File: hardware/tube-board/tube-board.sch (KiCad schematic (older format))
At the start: 8 parts

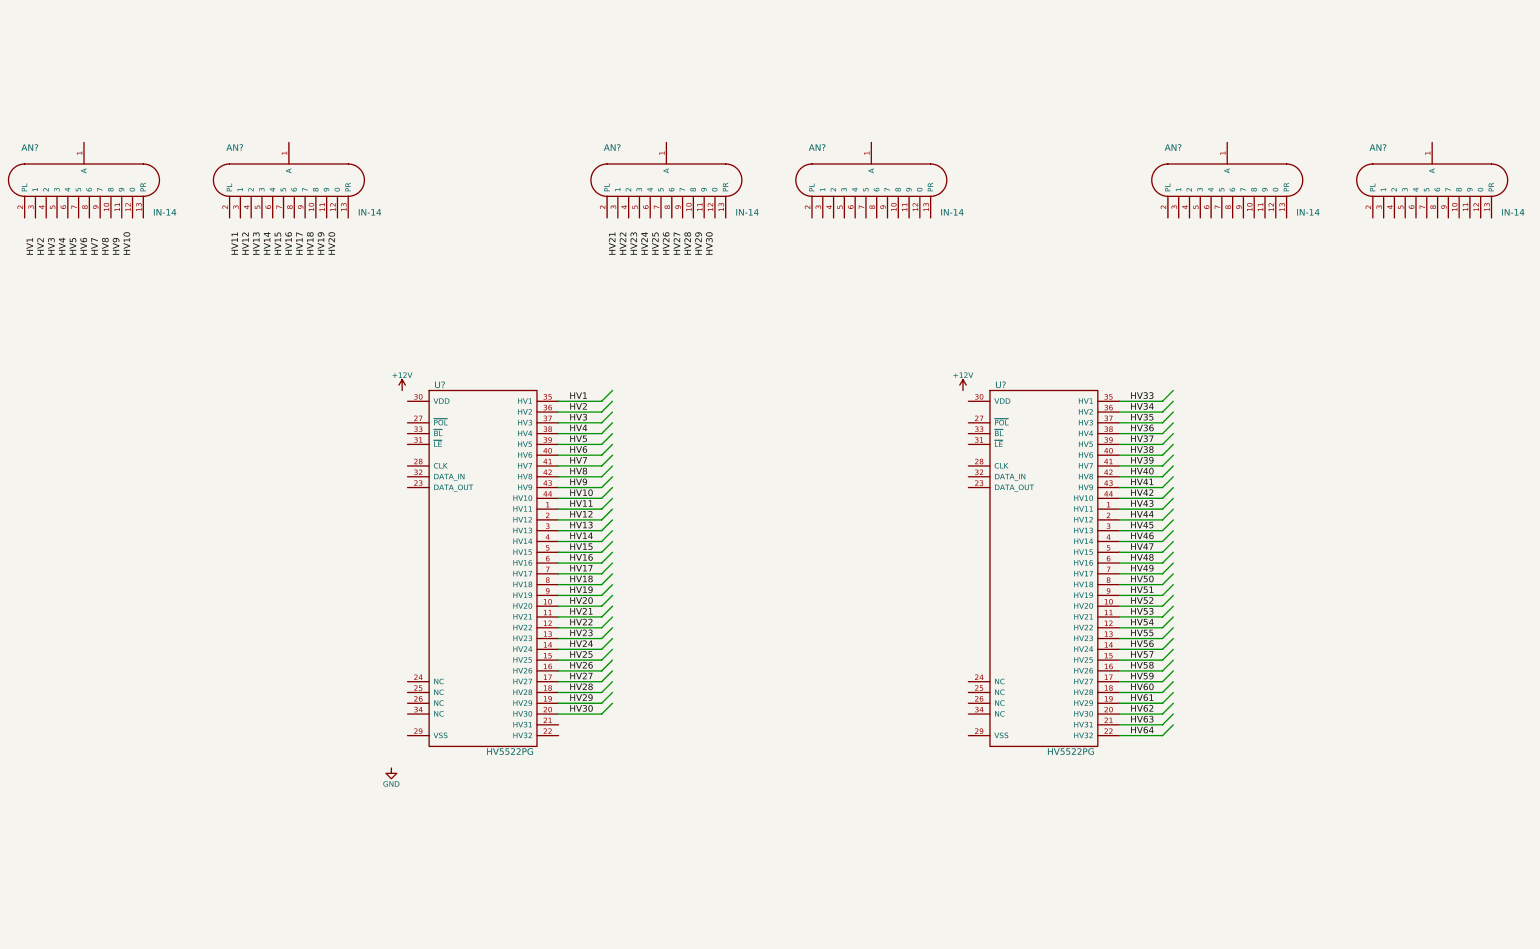
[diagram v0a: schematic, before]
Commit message: Working on tube board schematic
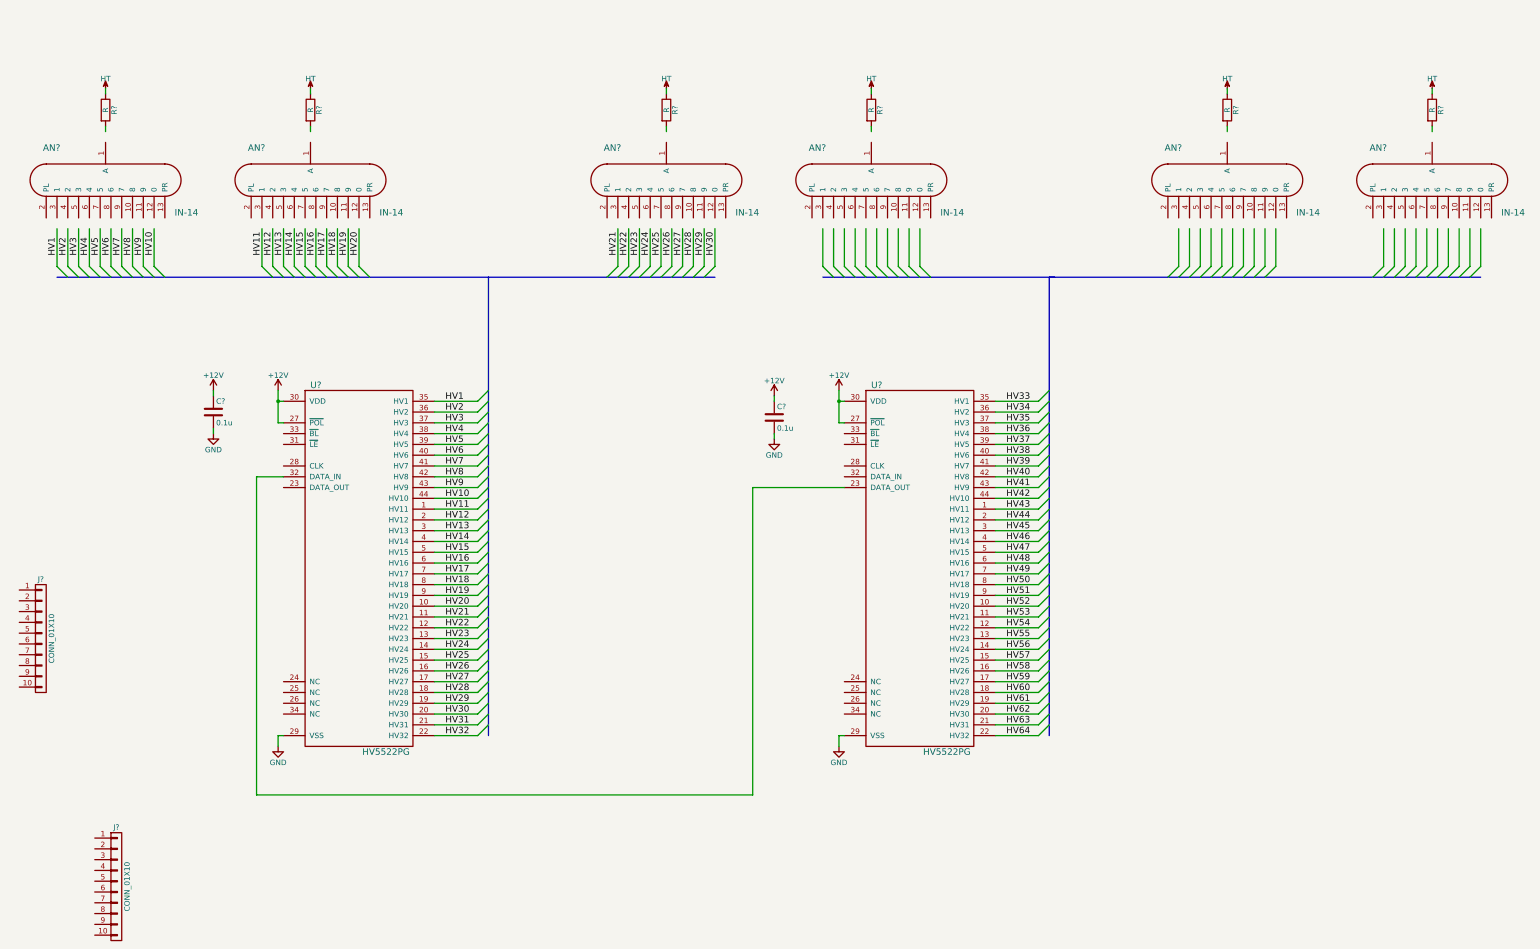
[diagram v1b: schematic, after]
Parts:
- added C? (x2): 0.1u, symbol C
- added J? (x2): CONN_01X10, symbol CONN_01X10
- added R? (x6): R, symbol R
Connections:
- net labels added: HT, HV31, HV32
- wire segments 62 -> 157
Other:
- moved on the sheet: AN?, U?

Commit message: Completed tube board schematic
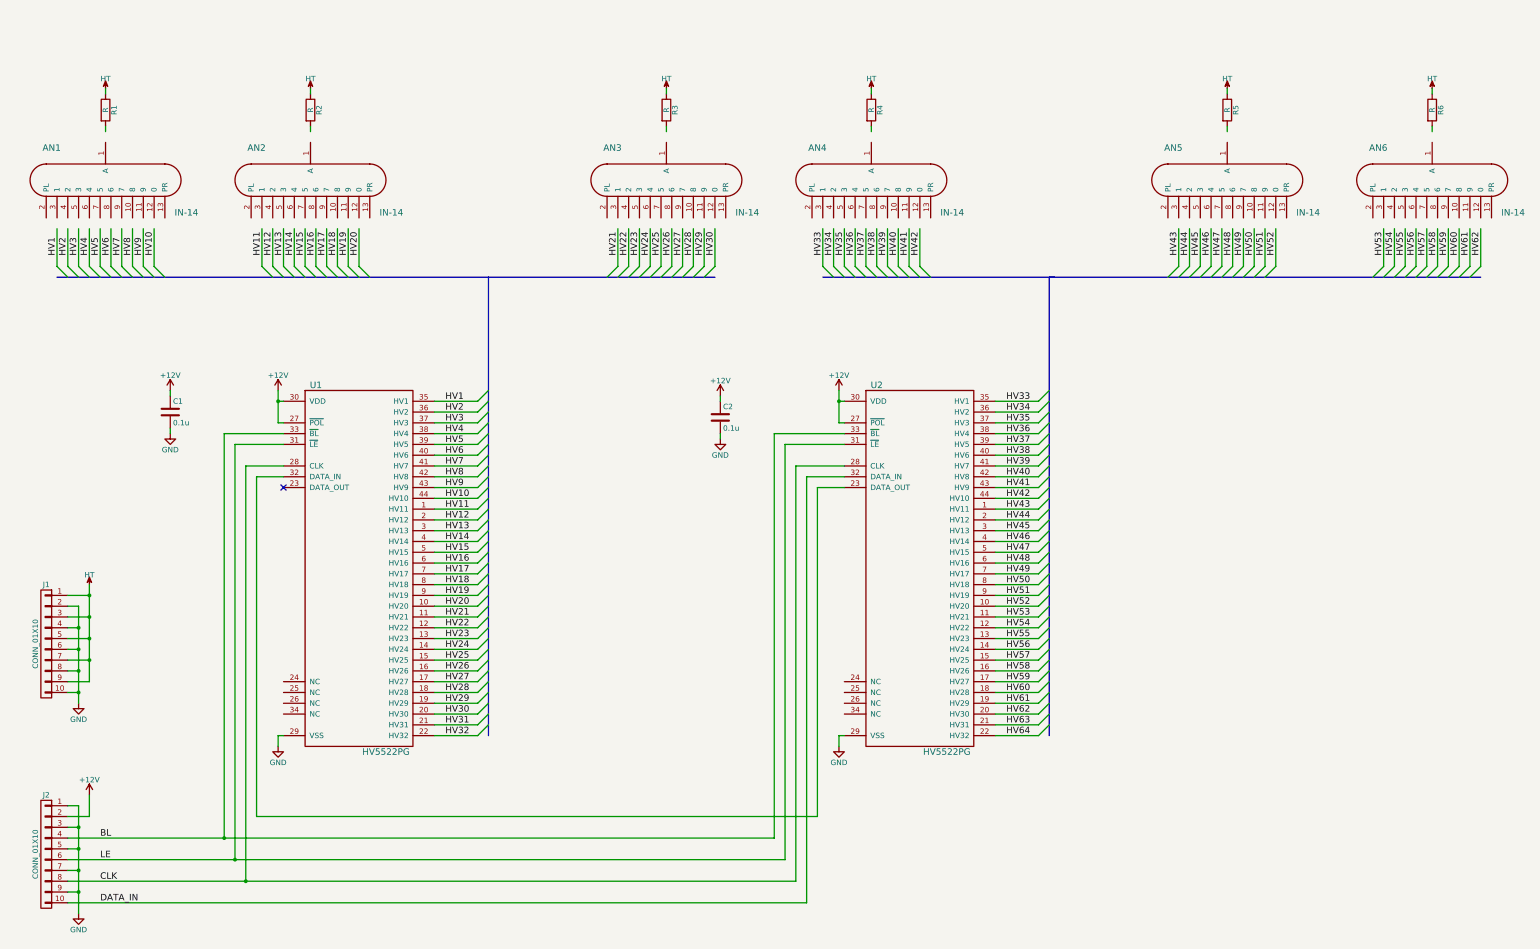
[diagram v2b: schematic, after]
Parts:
- gave numbers to parts that had none: 18
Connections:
- net labels added: BL, CLK, DATA_IN, LE
- wire segments 157 -> 193
- no-connect marks 0 -> 1
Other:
- moved on the sheet: C1, C2, J1, J2

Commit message: Working on footprints
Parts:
- C1, C2: footprint (none) -> Capacitors_SMD:C_0603; Source (none) -> DigiKey
- R1, R2, R3, R4, R5, R6: value R -> 8.2k; footprint (none) -> Resistors_SMD:R_1206; Part (none) -> 311-8.20KFRCT-ND; Source (none) -> DigiKey
- U1, U2: footprint (none) -> Housings_QFP:LQFP-44_10x10mm_Pitch0.8mm; Source (none) -> DigiKey
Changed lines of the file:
@@
 F 0 "U2" H 9450 7750 60  0000 C CNN
 F 1 "HV5522PG" H 10100 4350 60  0000 C CNN
-F 2 "" H 9850 6050 60  0001 C CNN
+F 2 "Housings_QFP:LQFP-44_10x10mm_Pitch0.8mm" H 9850 6050 60  0001 C CNN
 F 3 "" H 9850 6050 60  0001 C CNN
+F 4 "DigiKey" H 9850 6050 60  0001 C CNN "Source"
 	1    9850 6050
 	1    0    0    -1
@@
 F 0 "U1" H 4250 7750 60  0000 C CNN
 F 1 "HV5522PG" H 4900 4350 60  0000 C CNN
-F 2 "" H 4650 6050 60  0001 C CNN
+F 2 "Housings_QFP:LQFP-44_10x10mm_Pitch0.8mm" H 4650 6050 60  0001 C CNN
 F 3 "" H 4650 6050 60  0001 C CNN
+F 4 "DigiKey" H 4650 6050 60  0001 C CNN "Source"
 	1    4650 6050
 	1    0    0    -1
@@
 P 2300 1800
 F 0 "R1" V 2380 1800 50  0000 C CNN
-F 1 "R" V 2300 1800 50  0000 C CNN
-F 2 "" V 2230 1800 50  0001 C CNN
+F 1 "8.2k" V 2300 1800 50  0000 C CNN
+F 2 "Resistors_SMD:R_1206" V 2230 1800 50  0001 C CNN
 F 3 "" H 2300 1800 50  0001 C CNN
+F 4 "DigiKey" H 2300 1800 60  0001 C CNN "Source"
+F 5 "311-8.20KFRCT-ND" H 2300 1800 60  0001 C CNN "Part"
 	1    2300 1800
 	1    0    0    -1
@@
 $EndComp
 $Comp
-L R R2
-U 1 1 58E1157E
-P 4200 1800
-F 0 "R2" V 4280 1800 50  0000 C CNN
-F 1 "R" V 4200 1800 50  0000 C CNN
-F 2 "" V 4130 1800 50  0001 C CNN
-F 3 "" H 4200 1800 50  0001 C CNN
-	1    4200 1800
-	1    0    0    -1
-$EndComp
-$Comp
 L HT #PWR10
 U 1 1 58E11584
@@
 $EndComp
 $Comp
-L R R3
-U 1 1 58E11609
-P 7500 1800
-F 0 "R3" V 7580 1800 50  0000 C CNN
-F 1 "R" V 7500 1800 50  0000 C CNN
-F 2 "" V 7430 1800 50  0001 C CNN
-F 3 "" H 7500 1800 50  0001 C CNN
-	1    7500 1800
-	1    0    0    -1
-$EndComp
-$Comp
 L HT #PWR11
 U 1 1 58E1160F
@@
 $EndComp
 $Comp
-L R R4
-U 1 1 58E11835
-P 9400 1800
-F 0 "R4" V 9480 1800 50  0000 C CNN
-F 1 "R" V 9400 1800 50  0000 C CNN
-F 2 "" V 9330 1800 50  0001 C CNN
-F 3 "" H 9400 1800 50  0001 C CNN
-	1    9400 1800
-	1    0    0    -1
-$EndComp
-$Comp
 L HT #PWR16
 U 1 1 58E1183B
@@
 $EndComp
 $Comp
-L R R5
-U 1 1 58E11870
-P 12700 1800
-F 0 "R5" V 12780 1800 50  0000 C CNN
-F 1 "R" V 12700 1800 50  0000 C CNN
-F 2 "" V 12630 1800 50  0001 C CNN
-F 3 "" H 12700 1800 50  0001 C CNN
-	1    12700 1800
-	1    0    0    -1
-$EndComp
-$Comp
 L HT #PWR17
 U 1 1 58E11876
@@
 $EndComp
 $Comp
-L R R6
-U 1 1 58E11B0B
-P 14600 1800
-F 0 "R6" V 14680 1800 50  0000 C CNN
-F 1 "R" V 14600 1800 50  0000 C CNN
-F 2 "" V 14530 1800 50  0001 C CNN
-F 3 "" H 14600 1800 50  0001 C CNN
-	1    14600 1800
-	1    0    0    -1
-$EndComp
-$Comp
 L HT #PWR18
 U 1 1 58E11B11
@@
 F 0 "C1" H 2925 4700 50  0000 L CNN
 F 1 "0.1u" H 2925 4500 50  0000 L CNN
-F 2 "" H 2938 4450 50  0001 C CNN
+F 2 "Capacitors_SMD:C_0603" H 2938 4450 50  0001 C CNN
 F 3 "" H 2900 4600 50  0001 C CNN
+F 4 "DigiKey" H 2900 4600 60  0001 C CNN "Source"
 	1    2900 4600
 	1    0    0    -1
@@
 F 0 "C2" H 8025 4750 50  0000 L CNN
 F 1 "0.1u" H 8025 4550 50  0000 L CNN
-F 2 "" H 8038 4500 50  0001 C CNN
+F 2 "Capacitors_SMD:C_0603" H 8038 4500 50  0001 C CNN
 F 3 "" H 8000 4650 50  0001 C CNN
+F 4 "DigiKey" H 8000 4650 60  0001 C CNN "Source"
 	1    8000 4650
 	1    0    0    -1
@@
 Text Label 15050 3150 1    60   ~ 0
 HV62
+$Comp
+L R R2
+U 1 1 58E213AC
+P 4200 1800
+F 0 "R2" V 4280 1800 50  0000 C CNN
+F 1 "8.2k" V 4200 1800 50  0000 C CNN
+F 2 "Resistors_SMD:R_1206" V 4130 1800 50  0001 C CNN
+F 3 "" H 4200 1800 50  0001 C CNN
+F 4 "DigiKey" H 4200 1800 60  0001 C CNN "Source"
+F 5 "311-8.20KFRCT-ND" H 4200 1800 60  0001 C CNN "Part"
+	1    4200 1800
+	1    0    0    -1
+$EndComp
+$Comp
+L R R3
+U 1 1 58E213F9
+P 7500 1800
+F 0 "R3" V 7580 1800 50  0000 C CNN
+F 1 "8.2k" V 7500 1800 50  0000 C CNN
+F 2 "Resistors_SMD:R_1206" V 7430 1800 50  0001 C CNN
+F 3 "" H 7500 1800 50  0001 C CNN
+F 4 "DigiKey" H 7500 1800 60  0001 C CNN "Source"
+F 5 "311-8.20KFRCT-ND" H 7500 1800 60  0001 C CNN "Part"
+	1    7500 1800
+	1    0    0    -1
+$EndComp
+$Comp
+L R R4
+U 1 1 58E216F6
+P 9400 1800
+F 0 "R4" V 9480 1800 50  0000 C CNN
+F 1 "8.2k" V 9400 1800 50  0000 C CNN
+F 2 "Resistors_SMD:R_1206" V 9330 1800 50  0001 C CNN
+F 3 "" H 9400 1800 50  0001 C CNN
+F 4 "DigiKey" H 9400 1800 60  0001 C CNN "Source"
+F 5 "311-8.20KFRCT-ND" H 9400 1800 60  0001 C CNN "Part"
+	1    9400 1800
+	1    0    0    -1
+$EndComp
+$Comp
+L R R5
+U 1 1 58E21743
+P 12700 1800
+F 0 "R5" V 12780 1800 50  0000 C CNN
+F 1 "8.2k" V 12700 1800 50  0000 C CNN
+F 2 "Resistors_SMD:R_1206" V 12630 1800 50  0001 C CNN
+F 3 "" H 12700 1800 50  0001 C CNN
+F 4 "DigiKey" H 12700 1800 60  0001 C CNN "Source"
+F 5 "311-8.20KFRCT-ND" H 12700 1800 60  0001 C CNN "Part"
+	1    12700 1800
+	1    0    0    -1
+$EndComp
+$Comp
+L R R6
+U 1 1 58E21980
+P 14600 1800
+F 0 "R6" V 14680 1800 50  0000 C CNN
+F 1 "8.2k" V 14600 1800 50  0000 C CNN
+F 2 "Resistors_SMD:R_1206" V 14530 1800 50  0001 C CNN
+F 3 "" H 14600 1800 50  0001 C CNN
+F 4 "DigiKey" H 14600 1800 60  0001 C CNN "Source"
+F 5 "311-8.20KFRCT-ND" H 14600 1800 60  0001 C CNN "Part"
+	1    14600 1800
+	1    0    0    -1
+$EndComp
 $EndSCHEMATC

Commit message: Working on footprints
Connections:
- wire segments 193 -> 210
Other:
- moved on the sheet: AN1, AN2, AN3, AN4, AN5, AN6, C1, C2, J1, J2, R1, R2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

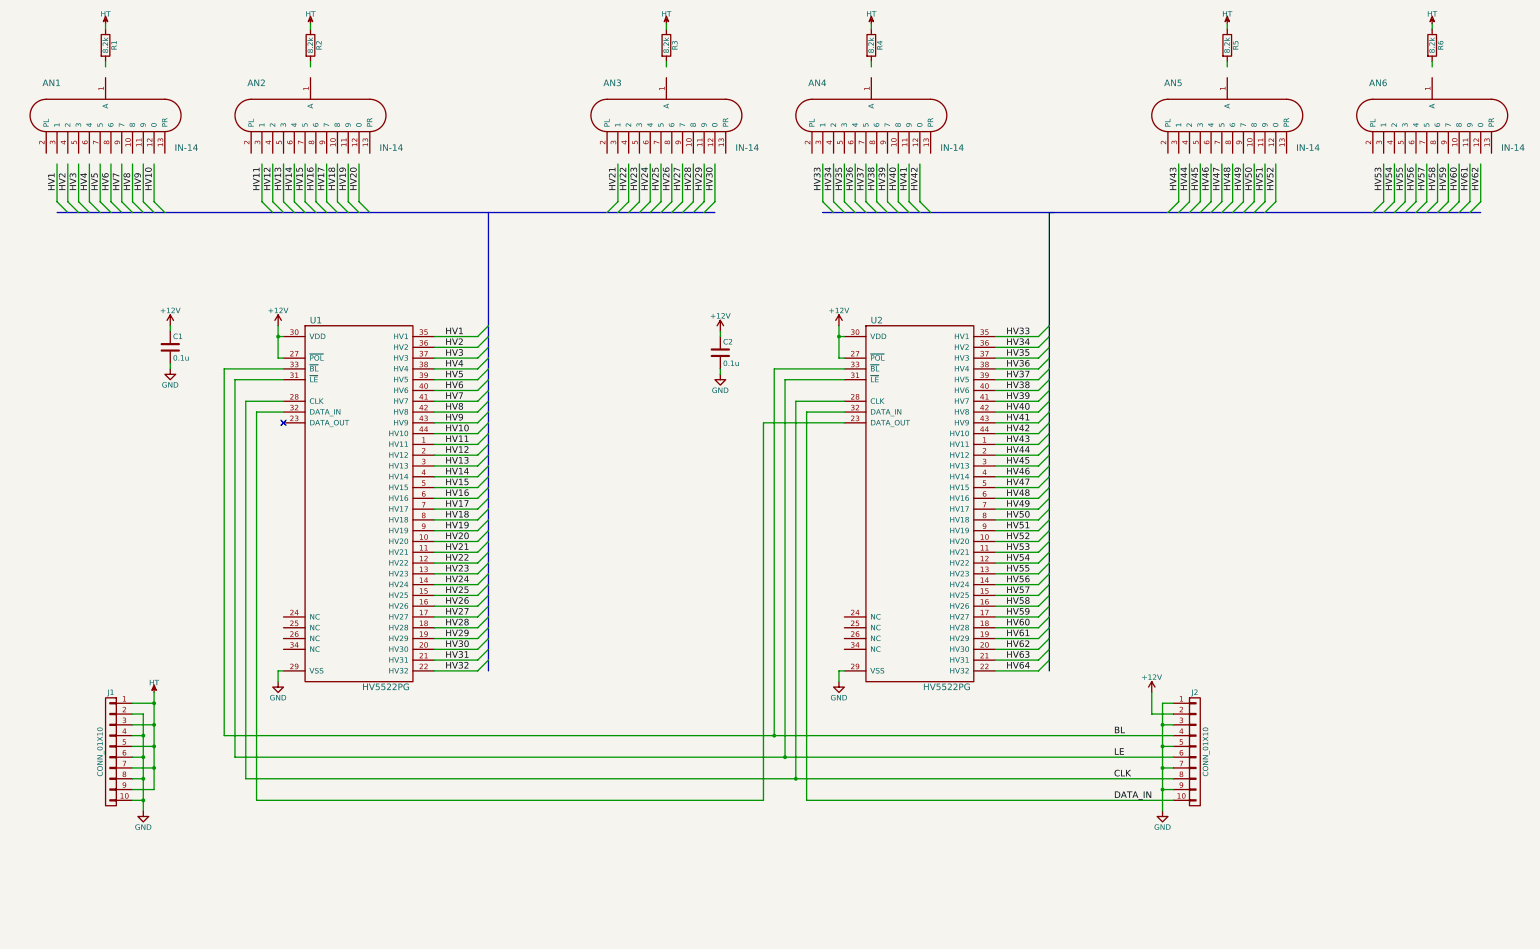
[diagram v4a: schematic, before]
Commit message: Working on tube board layout
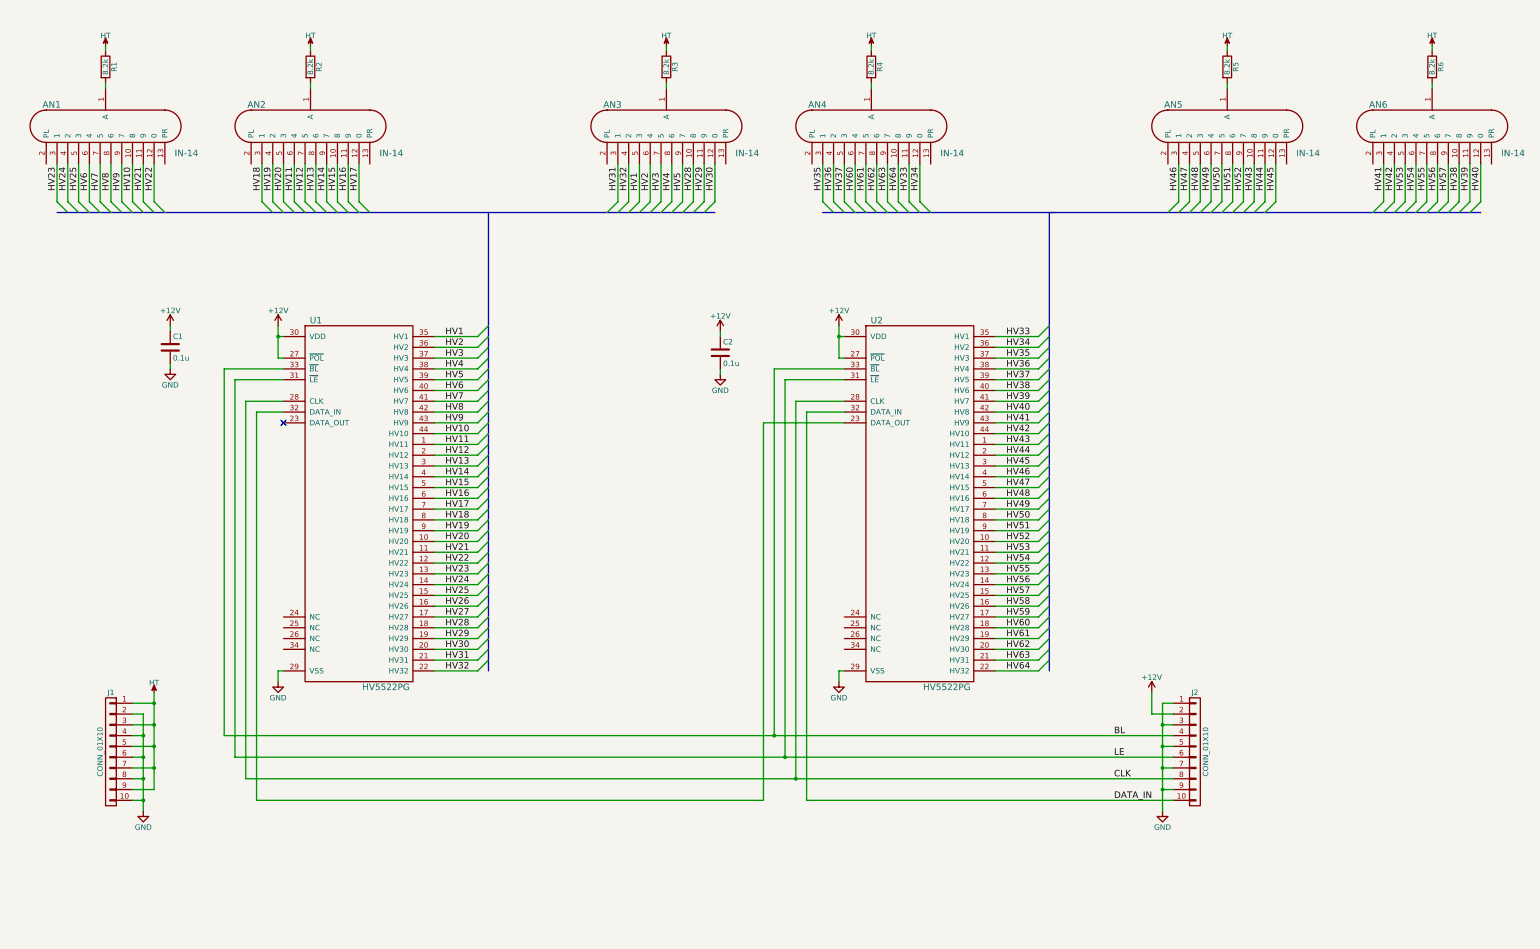
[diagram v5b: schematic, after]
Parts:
- AN1, AN2, AN3, AN4, AN5, AN6: footprint (none) -> radio-clock:IN-14; Source (none) -> DigiKey
- J1, J2: footprint (none) -> radio-clock:1-338728-0; Part (none) -> A116183CT-ND; Source (none) -> DigiKey
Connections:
- wire segments 210 -> 193
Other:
- moved on the sheet: AN1, AN2, AN3, AN4, AN5, AN6, R1, R2, R3, R4, R5, R6

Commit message: Finished tube board
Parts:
- C1, C2: footprint Capacitors_SMD:C_0603 -> Capacitors_SMD:C_0805
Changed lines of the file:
@@
 F 0 "C1" H 2925 4100 50  0000 L CNN
 F 1 "0.1u" H 2925 3900 50  0000 L CNN
-F 2 "Capacitors_SMD:C_0603" H 2938 3850 50  0001 C CNN
+F 2 "Capacitors_SMD:C_0805" H 2938 3850 50  0001 C CNN
 F 3 "" H 2900 4000 50  0001 C CNN
 F 4 "DigiKey" H 2900 4000 60  0001 C CNN "Source"
@@
 F 0 "C2" H 8025 4150 50  0000 L CNN
 F 1 "0.1u" H 8025 3950 50  0000 L CNN
-F 2 "Capacitors_SMD:C_0603" H 8038 3900 50  0001 C CNN
+F 2 "Capacitors_SMD:C_0805" H 8038 3900 50  0001 C CNN
 F 3 "" H 8000 4050 50  0001 C CNN
 F 4 "DigiKey" H 8000 4050 60  0001 C CNN "Source"
